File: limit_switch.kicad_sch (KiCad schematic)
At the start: 28 parts, among them U1 LTV-817S, U2 LTV-817S, U3 LTV-817S, U4 LTV-817S, U5 LTV-817S, U6 LTV-817S, U7 LTV-817S

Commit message: Version 1.1 - reworked all smd's to 0603
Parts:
- R1, R10, R11, R12, R13, R14, R2, R3, R4, R5, R6, R7, R8, R9: footprint Resistor_SMD:R_0201_0603Metric_Pad0.64x0.40mm_HandSolder -> Resistor_SMD:R_0603_1608Metric_Pad0.98x0.95mm_HandSolder
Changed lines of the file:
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@@
       (effects (font (size 1.27 1.27)) (justify left))
     )
-    (property "Footprint" "Resistor_SMD:R_0201_0603Metric_Pad0.64x0.40mm_HandSolder" (at 129.032 72.39 90)
+    (property "Footprint" "Resistor_SMD:R_0603_1608Metric_Pad0.98x0.95mm_HandSolder" (at 129.032 72.39 90)
       (effects (font (size 1.27 1.27)) hide)
     )
@@
       (effects (font (size 1.27 1.27)) (justify left))
     )
-    (property "Footprint" "Resistor_SMD:R_0201_0603Metric_Pad0.64x0.40mm_HandSolder" (at 65.532 134.62 90)
+    (property "Footprint" "Resistor_SMD:R_0603_1608Metric_Pad0.98x0.95mm_HandSolder" (at 65.532 134.62 90)
       (effects (font (size 1.27 1.27)) hide)
     )
@@
       (effects (font (size 1.27 1.27)) (justify left))
     )
-    (property "Footprint" "Resistor_SMD:R_0201_0603Metric_Pad0.64x0.40mm_HandSolder" (at 233.172 54.61 90)
+    (property "Footprint" "Resistor_SMD:R_0603_1608Metric_Pad0.98x0.95mm_HandSolder" (at 233.172 54.61 90)
       (effects (font (size 1.27 1.27)) hide)
     )
@@
       (effects (font (size 1.27 1.27)) (justify left))
     )
-    (property "Footprint" "Resistor_SMD:R_0201_0603Metric_Pad0.64x0.40mm_HandSolder" (at 258.572 72.39 90)
+    (property "Footprint" "Resistor_SMD:R_0603_1608Metric_Pad0.98x0.95mm_HandSolder" (at 258.572 72.39 90)
       (effects (font (size 1.27 1.27)) hide)
     )
@@
       (effects (font (size 1.27 1.27)) (justify left))
     )
-    (property "Footprint" "Resistor_SMD:R_0201_0603Metric_Pad0.64x0.40mm_HandSolder" (at 258.572 127 90)
+    (property "Footprint" "Resistor_SMD:R_0603_1608Metric_Pad0.98x0.95mm_HandSolder" (at 258.572 127 90)
       (effects (font (size 1.27 1.27)) hide)
     )
@@
       (effects (font (size 1.27 1.27)) (justify left))
     )
-    (property "Footprint" "Resistor_SMD:R_0201_0603Metric_Pad0.64x0.40mm_HandSolder" (at 103.632 54.61 90)
+    (property "Footprint" "Resistor_SMD:R_0603_1608Metric_Pad0.98x0.95mm_HandSolder" (at 103.632 54.61 90)
       (effects (font (size 1.27 1.27)) hide)
     )
@@
       (effects (font (size 1.27 1.27)) (justify left))
     )
-    (property "Footprint" "Resistor_SMD:R_0201_0603Metric_Pad0.64x0.40mm_HandSolder" (at 106.172 115.57 90)
+    (property "Footprint" "Resistor_SMD:R_0603_1608Metric_Pad0.98x0.95mm_HandSolder" (at 106.172 115.57 90)
       (effects (font (size 1.27 1.27)) hide)
     )
@@
       (effects (font (size 1.27 1.27)) (justify left))
     )
-    (property "Footprint" "Resistor_SMD:R_0201_0603Metric_Pad0.64x0.40mm_HandSolder" (at 37.592 54.61 90)
+    (property "Footprint" "Resistor_SMD:R_0603_1608Metric_Pad0.98x0.95mm_HandSolder" (at 37.592 54.61 90)
       (effects (font (size 1.27 1.27)) hide)
     )
@@
       (effects (font (size 1.27 1.27)) (justify left))
     )
-    (property "Footprint" "Resistor_SMD:R_0201_0603Metric_Pad0.64x0.40mm_HandSolder" (at 62.992 72.39 90)
+    (property "Footprint" "Resistor_SMD:R_0603_1608Metric_Pad0.98x0.95mm_HandSolder" (at 62.992 72.39 90)
       (effects (font (size 1.27 1.27)) hide)
     )
@@
       (effects (font (size 1.27 1.27)) (justify left))
     )
-    (property "Footprint" "Resistor_SMD:R_0201_0603Metric_Pad0.64x0.40mm_HandSolder" (at 40.132 116.84 90)
+    (property "Footprint" "Resistor_SMD:R_0603_1608Metric_Pad0.98x0.95mm_HandSolder" (at 40.132 116.84 90)
       (effects (font (size 1.27 1.27)) hide)
     )
@@
       (effects (font (size 1.27 1.27)) (justify left))
     )
-    (property "Footprint" "Resistor_SMD:R_0201_0603Metric_Pad0.64x0.40mm_HandSolder" (at 193.802 72.39 90)
+    (property "Footprint" "Resistor_SMD:R_0603_1608Metric_Pad0.98x0.95mm_HandSolder" (at 193.802 72.39 90)
       (effects (font (size 1.27 1.27)) hide)
     )
@@
       (effects (font (size 1.27 1.27)) (justify left))
     )
-    (property "Footprint" "Resistor_SMD:R_0201_0603Metric_Pad0.64x0.40mm_HandSolder" (at 233.172 109.22 90)
+    (property "Footprint" "Resistor_SMD:R_0603_1608Metric_Pad0.98x0.95mm_HandSolder" (at 233.172 109.22 90)
       (effects (font (size 1.27 1.27)) hide)
     )
@@
       (effects (font (size 1.27 1.27)) (justify left))
     )
-    (property "Footprint" "Resistor_SMD:R_0201_0603Metric_Pad0.64x0.40mm_HandSolder" (at 131.572 133.35 90)
+    (property "Footprint" "Resistor_SMD:R_0603_1608Metric_Pad0.98x0.95mm_HandSolder" (at 131.572 133.35 90)
       (effects (font (size 1.27 1.27)) hide)
     )
@@
       (effects (font (size 1.27 1.27)) (justify left))
     )
-    (property "Footprint" "Resistor_SMD:R_0201_0603Metric_Pad0.64x0.40mm_HandSolder" (at 168.402 54.61 90)
-      (effects (font (size 1.27 1.27)) hide)
-    )
+    (property "Footprint" "Resistor_SMD:R_0603_1608Metric_Pad0.98x0.95mm_HandSolder" (at 168.402 54.61 90)
+      (effects (font (size 1.27 1.27)) hide)
+    )

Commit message: Updating for version 1.1
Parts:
- added H5: MountingHole_Pad, MountingHole:MountingHole_3mm_Pad, symbol Mechanical:MountingHole_Pad
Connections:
- net GND: now also H5.1
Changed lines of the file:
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@@
+    (stroke (width 0) (type default))
+  )
+  (wire (pts (xy 58.42 167.64) (xy 58.42 171.45))
     (stroke (width 0) (type default))
   )
@@
     )
   )
+  (symbol (lib_id "power:GND") (at 58.42 171.45 0) (unit 1)
+    (in_bom yes) (on_board yes) (dnp no) (fields_autoplaced)
+    (property "Reference" "#PWR0137" (at 58.42 177.8 0)
+      (effects (font (size 1.27 1.27)) hide)
+    )
+    (property "Value" "GND" (at 58.42 176.53 0)
+      (effects (font (size 1.27 1.27)))
+    )
+    (property "Footprint" "" (at 58.42 171.45 0)
+      (effects (font (size 1.27 1.27)) hide)
+    )
+    (property "Datasheet" "" (at 58.42 171.45 0)
+      (effects (font (size 1.27 1.27)) hide)
+    )
+    (pin "1")
+    (instances
+      (project "stm_bob"
+        (path "/fe5b111f-0cc6-4899-bf0b-69fcfcbfb6c3/f1e2d5d9-a14c-4b74-a15c-c4917cefb81f"
+          (reference "#PWR0137") (unit 1)
+        )
+      )
+    )
+  )
   (symbol (lib_id "power:+12V") (at 35.56 111.76 0) (unit 1)
     (in_bom yes) (on_board yes) (dnp no) (fields_autoplaced)
@@
         )
       )
+    )
+  )
+  (symbol (lib_id "Mechanical:MountingHole_Pad") (at 58.42 165.1 0) (unit 1)
+    (in_bom yes) (on_board yes) (dnp no) (fields_autoplaced)
+    (property "Reference" "H5" (at 60.96 162.56 0)
+      (effects (font (size 1.27 1.27)) (justify left))
+    )
+    (property "Value" "MountingHole_Pad" (at 60.96 165.1 0)
+      (effects (font (size 1.27 1.27)) (justify left))
+    )
+    (property "Footprint" "MountingHole:MountingHole_3mm_Pad" (at 58.42 165.1 0)
+      (effects (font (size 1.27 1.27)) hide)
+    )
+    (property "Datasheet" "~" (at 58.42 165.1 0)
+      (effects (font (size 1.27 1.27)) hide)
+    )
+    (pin "1")
+    (instances
+      (project "stm_bob"
+        (path "/fe5b111f-0cc6-4899-bf0b-69fcfcbfb6c3/f1e2d5d9-a14c-4b74-a15c-c4917cefb81f"
+          (reference "H5") (unit 1)
+        )
+      )

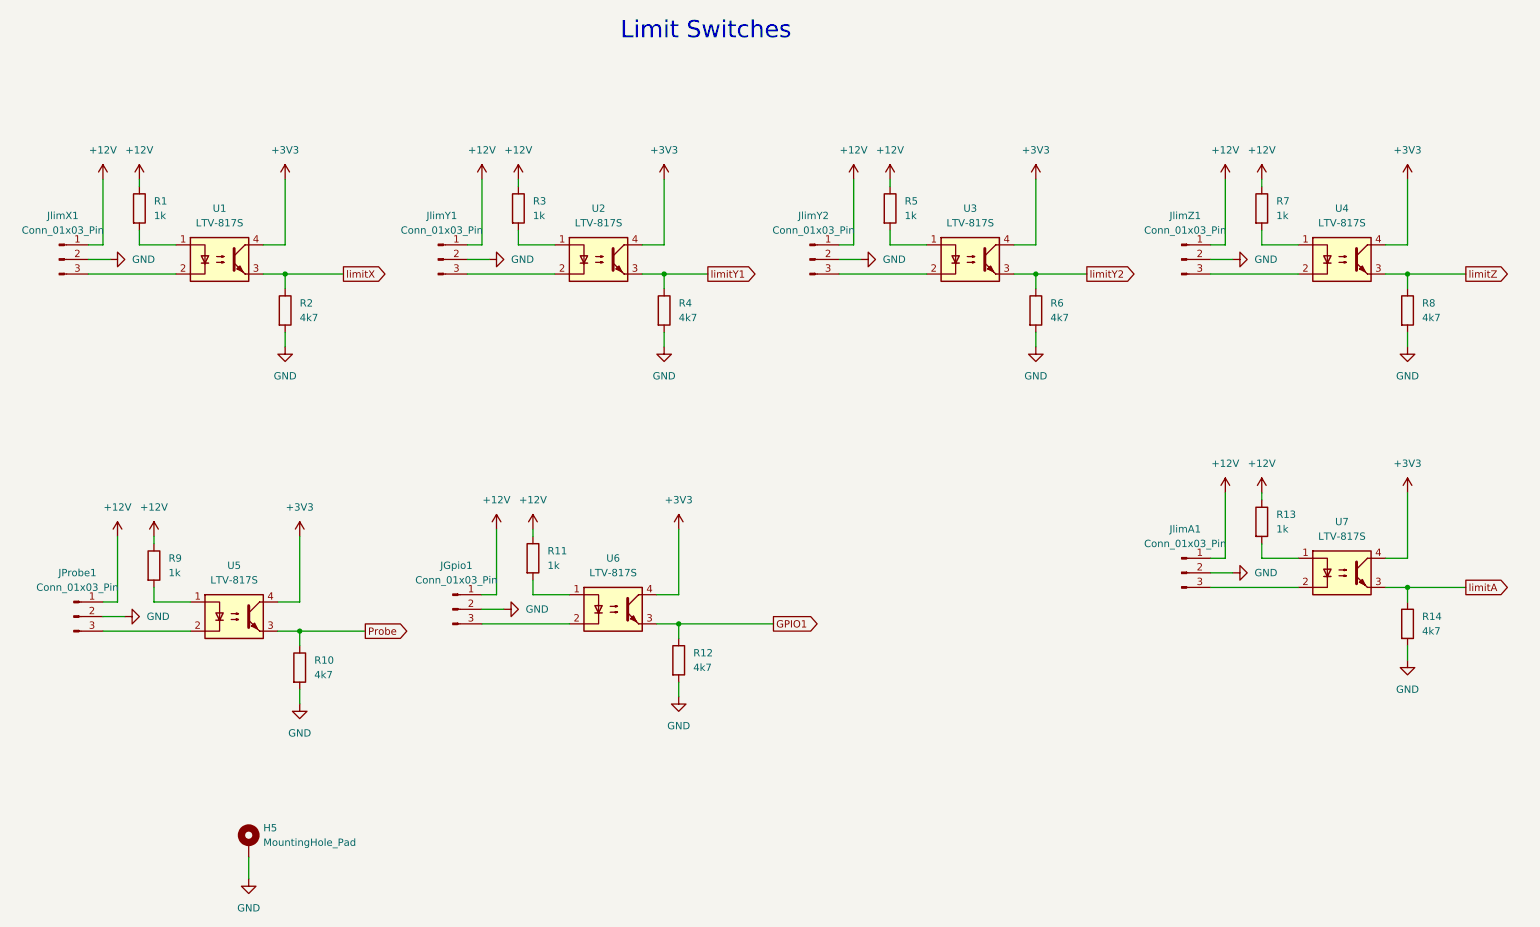
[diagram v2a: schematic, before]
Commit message: Mainly value updates
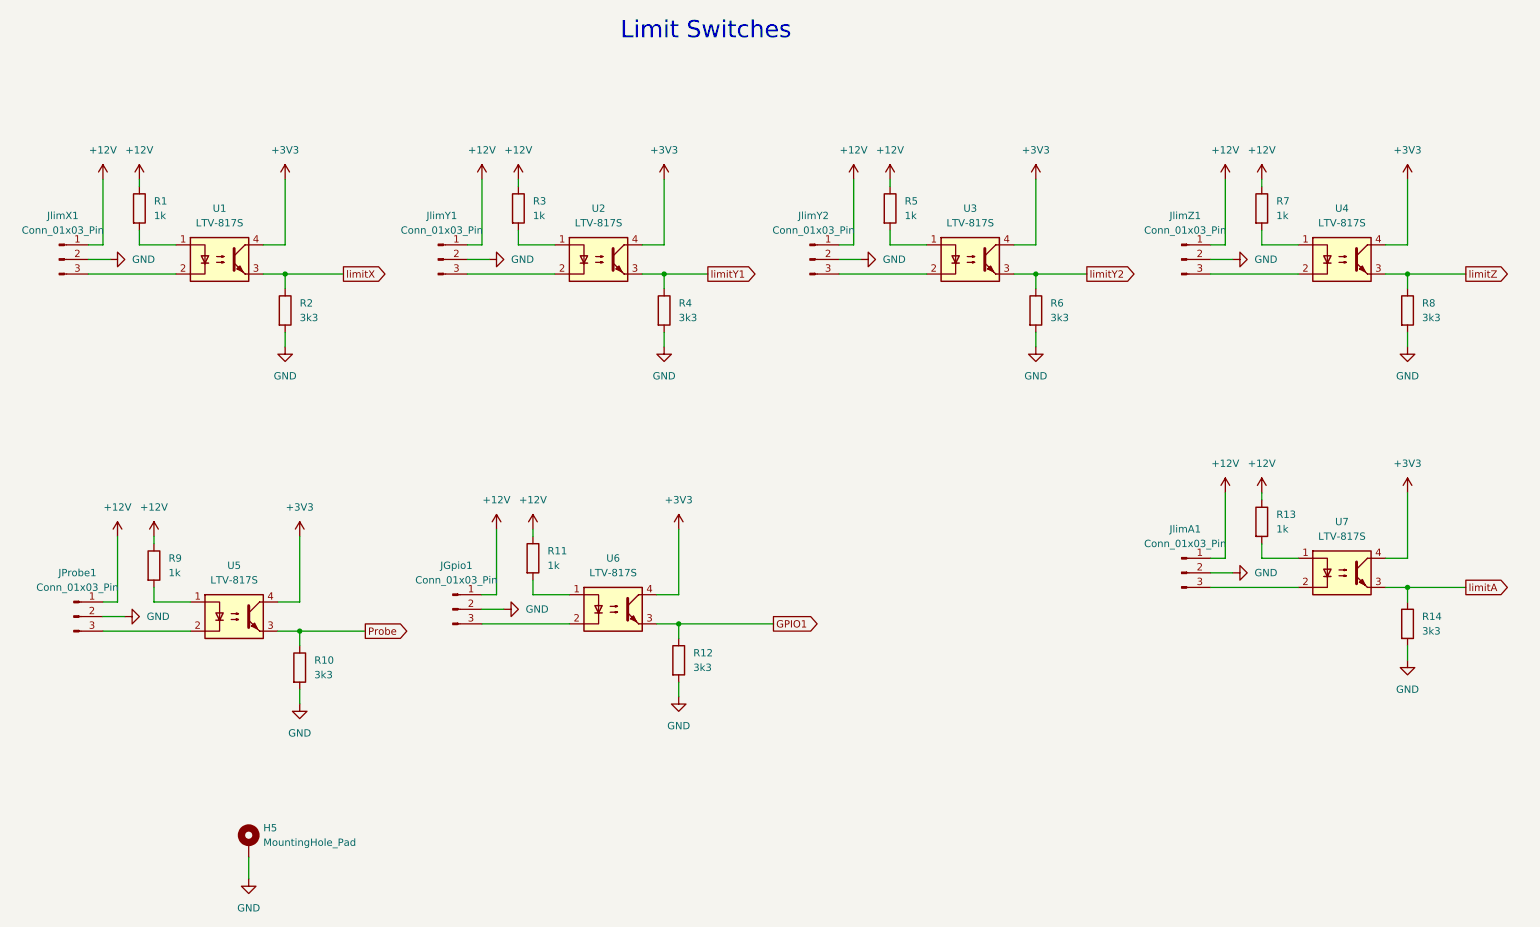
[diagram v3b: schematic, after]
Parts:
- R10, R12, R14, R2, R4, R6, R8: value 4k7 -> 3k3
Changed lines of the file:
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@@
       (effects (font (size 1.27 1.27)) (justify left))
     )
-    (property "Value" "4k7" (at 133.35 73.66 0)
+    (property "Value" "3k3" (at 133.35 73.66 0)
       (effects (font (size 1.27 1.27)) (justify left))
     )
@@
       (effects (font (size 1.27 1.27)) (justify left))
     )
-    (property "Value" "4k7" (at 69.85 135.89 0)
+    (property "Value" "3k3" (at 69.85 135.89 0)
       (effects (font (size 1.27 1.27)) (justify left))
     )
@@
       (effects (font (size 1.27 1.27)) (justify left))
     )
-    (property "Value" "4k7" (at 262.89 73.66 0)
+    (property "Value" "3k3" (at 262.89 73.66 0)
       (effects (font (size 1.27 1.27)) (justify left))
     )
@@
       (effects (font (size 1.27 1.27)) (justify left))
     )
-    (property "Value" "4k7" (at 262.89 128.27 0)
+    (property "Value" "3k3" (at 262.89 128.27 0)
       (effects (font (size 1.27 1.27)) (justify left))
     )
@@
       (effects (font (size 1.27 1.27)) (justify left))
     )
-    (property "Value" "4k7" (at 67.31 73.66 0)
+    (property "Value" "3k3" (at 67.31 73.66 0)
       (effects (font (size 1.27 1.27)) (justify left))
     )
@@
       (effects (font (size 1.27 1.27)) (justify left))
     )
-    (property "Value" "4k7" (at 198.12 73.66 0)
+    (property "Value" "3k3" (at 198.12 73.66 0)
       (effects (font (size 1.27 1.27)) (justify left))
     )
@@
       (effects (font (size 1.27 1.27)) (justify left))
     )
-    (property "Value" "4k7" (at 135.89 134.62 0)
-      (effects (font (size 1.27 1.27)) (justify left))
-    )
+    (property "Value" "3k3" (at 135.89 134.62 0)
+      (effects (font (size 1.27 1.27)) (justify left))
+    )
